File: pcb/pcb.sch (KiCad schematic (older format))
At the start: 30 parts, among them J1 Conn_01x01, J2 Conn_01x01, J3 Conn_01x01, J4 Conn_02x05_Odd_Even, J5 RJ45_Amphenol_RJMG1BD3B8K1ANR, J6 Conn_01x01, U1 ENC28J60x-SS, Y1 Crystal

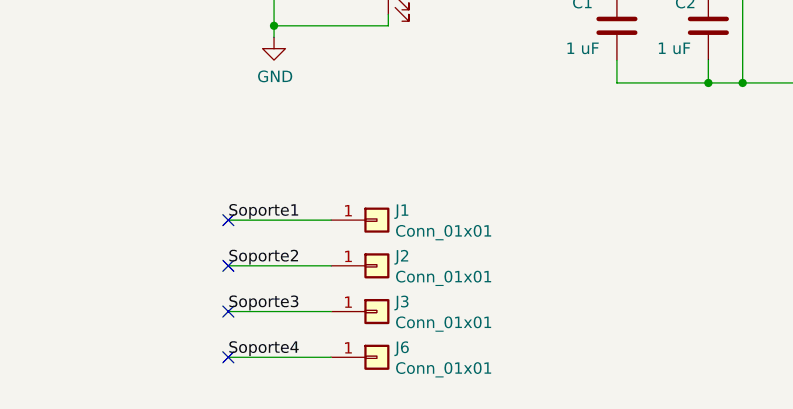
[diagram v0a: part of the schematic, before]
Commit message: Corrección de pin de montaje
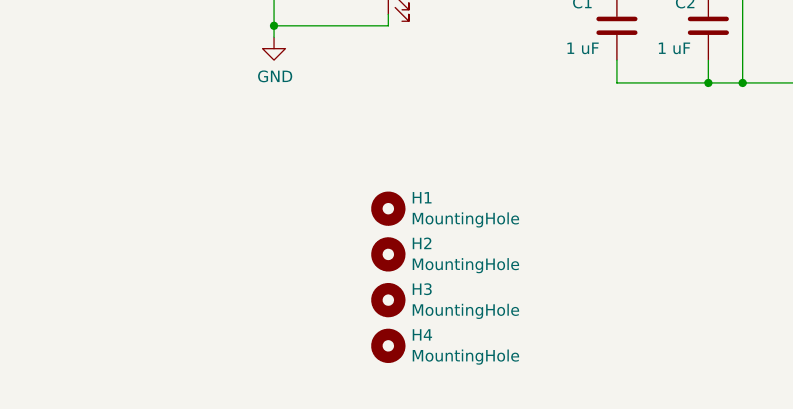
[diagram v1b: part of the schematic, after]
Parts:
- removed J1, J2, J3, J6: Conn_01x01, Connector_PinHeader_2.00mm:PinHeader_1x01_P2.00mm_Vertical, symbol Connector_Generic:Conn_01x01
- added H1, H2, H3, H4: MountingHole, MountingHole:MountingHole_2.2mm_M2_DIN965_Pad, symbol Mechanical:MountingHole
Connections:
- no-connect marks 4 -> 0
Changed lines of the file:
@@
-$EndComp
-$Comp
-L Connector_Generic:Conn_01x01 J1
-U 1 1 60E43515
-P 2250 4950
-F 0 "J1" H 2330 4992 50  0000 L CNN
-F 1 "Conn_01x01" H 2330 4901 50  0000 L CNN
-F 2 "Connector_PinHeader_2.00mm:PinHeader_1x01_P2.00mm_Vertical" H 2250 4950 50  0001 C CNN
-F 3 "~" H 2250 4950 50  0001 C CNN
-	1    2250 4950
-	1    0    0    -1
-$EndComp
-$Comp
-L Connector_Generic:Conn_01x01 J2
-U 1 1 60E43AF3
-P 2250 5150
-F 0 "J2" H 2330 5192 50  0000 L CNN
-F 1 "Conn_01x01" H 2330 5101 50  0000 L CNN
-F 2 "Connector_PinHeader_2.00mm:PinHeader_1x01_P2.00mm_Vertical" H 2250 5150 50  0001 C CNN
-F 3 "~" H 2250 5150 50  0001 C CNN
-	1    2250 5150
-	1    0    0    -1
-$EndComp
-$Comp
-L Connector_Generic:Conn_01x01 J3
-U 1 1 60E43C47
-P 2250 5350
-F 0 "J3" H 2330 5392 50  0000 L CNN
-F 1 "Conn_01x01" H 2330 5301 50  0000 L CNN
-F 2 "Connector_PinHeader_2.00mm:PinHeader_1x01_P2.00mm_Vertical" H 2250 5350 50  0001 C CNN
-F 3 "~" H 2250 5350 50  0001 C CNN
-	1    2250 5350
-	1    0    0    -1
 $EndComp
 $Comp
@@
 	1    0    0    -1
 $EndComp
-Text Label 1600 4950 0    50   ~ 0
-Soporte1
-Text Label 1600 5150 0    50   ~ 0
-Soporte2
-Text Label 1600 5350 0    50   ~ 0
-Soporte3
 $Comp
 L power:+3.3V #PWR01
@@
 	1    0    0    -1
 $EndComp
-Wire Wire Line
-	2050 4950 1600 4950
-Wire Wire Line
-	2050 5150 1600 5150
-Wire Wire Line
-	2050 5350 1600 5350
-NoConn ~ 1600 5350
-NoConn ~ 1600 5150
-NoConn ~ 1600 4950
 $Comp
 L power:PWR_FLAG #FLG0102
@@
 	3850 4350 4950 4350
 $Comp
-L Connector_Generic:Conn_01x01 J6
-U 1 1 60EAD1CE
-P 2250 5550
-F 0 "J6" H 2330 5592 50  0000 L CNN
-F 1 "Conn_01x01" H 2330 5501 50  0000 L CNN
-F 2 "Connector_PinHeader_2.00mm:PinHeader_1x01_P2.00mm_Vertical" H 2250 5550 50  0001 C CNN
-F 3 "~" H 2250 5550 50  0001 C CNN
-	1    2250 5550
-	1    0    0    -1
-$EndComp
-Text Label 1600 5550 0    50   ~ 0
-Soporte4
-NoConn ~ 1600 5550
-Wire Wire Line
-	1600 5550 2050 5550
+L Mechanical:MountingHole H1
+U 1 1 60FFAFFD
+P 2300 4900
+F 0 "H1" H 2400 4946 50  0000 L CNN
+F 1 "MountingHole" H 2400 4855 50  0000 L CNN
+F 2 "MountingHole:MountingHole_2.2mm_M2_DIN965_Pad" H 2300 4900 50  0001 C CNN
+F 3 "~" H 2300 4900 50  0001 C CNN
+	1    2300 4900
+	1    0    0    -1
+$EndComp
+$Comp
+L Mechanical:MountingHole H2
+U 1 1 61001DC3
+P 2300 5100
+F 0 "H2" H 2400 5146 50  0000 L CNN
+F 1 "MountingHole" H 2400 5055 50  0000 L CNN
+F 2 "MountingHole:MountingHole_2.2mm_M2_DIN965_Pad" H 2300 5100 50  0001 C CNN
+F 3 "~" H 2300 5100 50  0001 C CNN
+	1    2300 5100
+	1    0    0    -1
+$EndComp
+$Comp
+L Mechanical:MountingHole H3
+U 1 1 61002005
+P 2300 5300
+F 0 "H3" H 2400 5346 50  0000 L CNN
+F 1 "MountingHole" H 2400 5255 50  0000 L CNN
+F 2 "MountingHole:MountingHole_2.2mm_M2_DIN965_Pad" H 2300 5300 50  0001 C CNN
+F 3 "~" H 2300 5300 50  0001 C CNN
+	1    2300 5300
+	1    0    0    -1
+$EndComp
+$Comp
+L Mechanical:MountingHole H4
+U 1 1 61002195
+P 2300 5500
+F 0 "H4" H 2400 5546 50  0000 L CNN
+F 1 "MountingHole" H 2400 5455 50  0000 L CNN
+F 2 "MountingHole:MountingHole_2.2mm_M2_DIN965_Pad" H 2300 5500 50  0001 C CNN
+F 3 "~" H 2300 5500 50  0001 C CNN
+	1    2300 5500
+	1    0    0    -1
+$EndComp
 $EndSCHEMATC

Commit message: Correcciones
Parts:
- renumbered J4 to J1, J5 to J2
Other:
- note added: "Conector de entrada"
- note added: "Conector de salida RJ45"
- note added: "Controlador Ethernet"
- note added: "Fiducials"
- note added: "Led indicador de alimentación"
- note added: "Lineas de comunicación"
- note added: "Montaje"
- moved on the sheet: C6, D1, FID1, FID2, FID3, FID4, H1, H2, H3, H4, R5

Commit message: Mejoras en diseño
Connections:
- net TPIN_N: now reaches J2.R2 (TD-), R7.2, U1.12 (TPIN-)
- net TPIN_P: now reaches J2.R1 (TD+), R6.1, U1.13 (TPIN+)
- net TPOUT_N: now reaches J2.R6 (RD-), R9.2, U1.16 (TPOUT-)
- net TPOUT_P: now reaches J2.R3 (RD+), R8.1, U1.17 (TPOUT+)
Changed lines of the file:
@@
 Text Notes 6750 1850 0    59   ~ 12
 Lineas de comunicación
+Text Label 5950 2700 0    50   ~ 0
+TPIN_P
+Text Label 5950 2800 0    50   ~ 0
+TPIN_N
+Text Label 5950 3200 0    50   ~ 0
+TPOUT_P
+Text Label 5950 3300 0    50   ~ 0
+TPOUT_N
 $EndSCHEMATC
